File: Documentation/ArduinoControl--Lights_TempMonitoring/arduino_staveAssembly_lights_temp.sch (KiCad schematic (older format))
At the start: 31 parts, among them P1 Power, P2 Analog, P3 Digital, P4 Digital, P5 CONN_01X01, P6 CONN_01X01, P7 CONN_01X01, P8 CONN_01X01

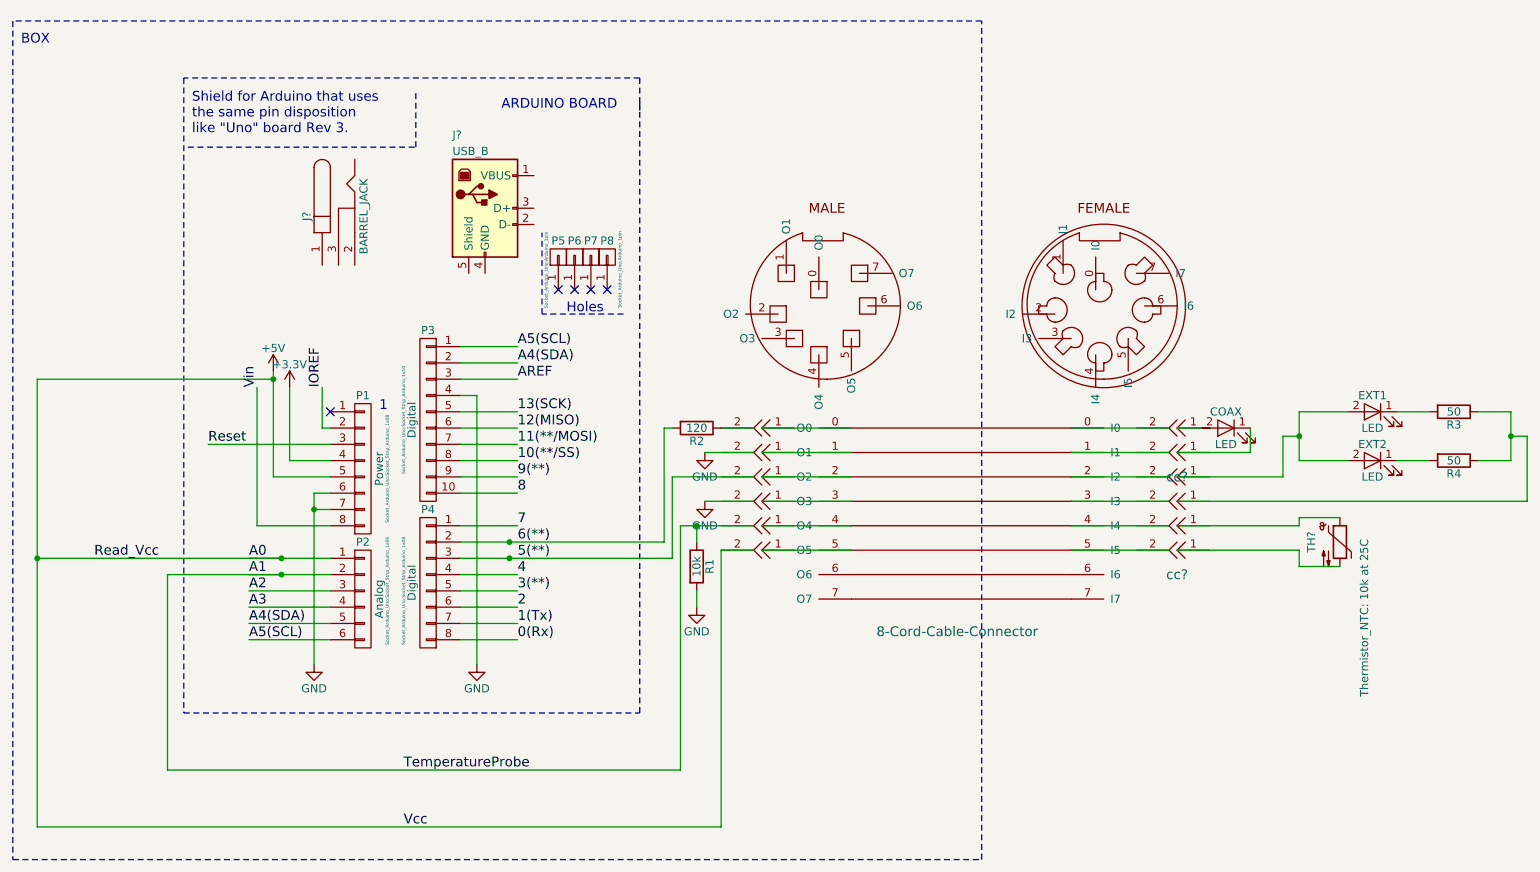
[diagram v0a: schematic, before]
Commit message: Arduino Lights system documentation
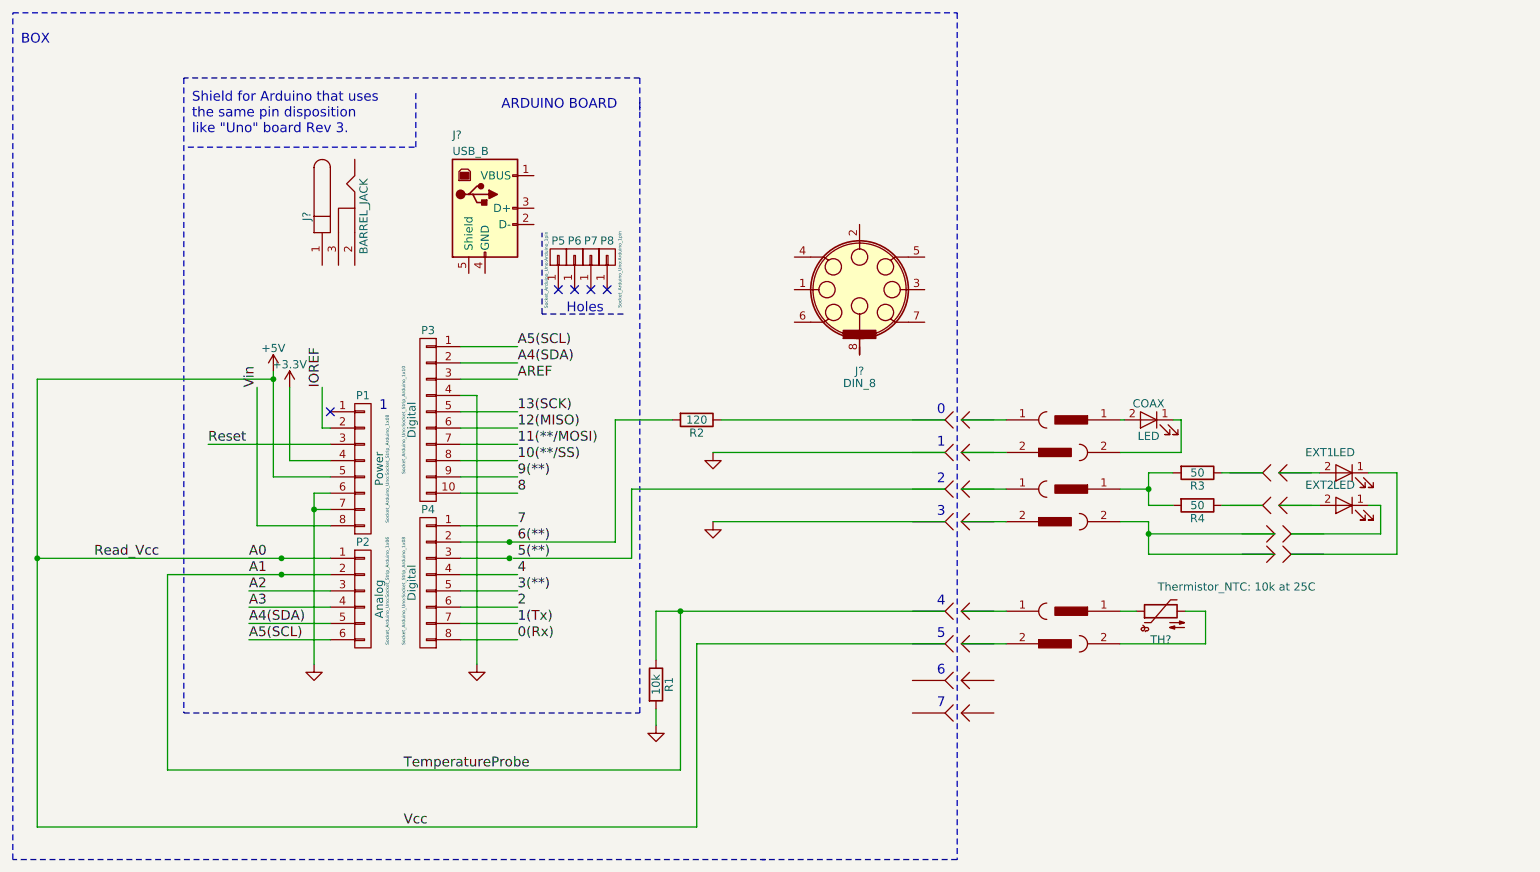
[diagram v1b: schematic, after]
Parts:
- removed U?: 8-Cord-Cable-Connector, symbol 8-Cord-Cable-Connector
- removed cc? (x12): single-wire connection, symbol Single-wire-connection
- added J?: DIN_8, symbol DIN_8
- added J? (x3): CONN_01X02_POL1, symbol CONN_01X02_POL1
- added J? (x3): CONN_01X02_POL2, symbol CONN_01X02_POL2
- added cc? (x12): Single-wire-connection-female, symbol Single-wire-connection-female
- added cc? (x12): Single-wire-connection-male, symbol Single-wire-connection-male
- COAX, EXT1, EXT2: Hotenda Part Number (none) -> H2886877
- TH?: DigiKey Part Number (none) -> 490-12820-ND
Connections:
- net +5V: now also cc?.~
- net 5(**): now also cc?.~; no longer P4.3 (P3)
- net A1: now also cc?.~
- net GND: now also cc?.~, cc?.~
- net at TH?.1: now also J?.1
- net at TH?.2: now also J?.2
- net at COAX.1 (K): now also J?.2
- net at COAX.2 (A): now also J?.1
- net at R3.1: now also cc?.~; no longer R4.1
- net at R3.2: now also R4.2, J?.1; no longer EXT1.1 (K)
- net at EXT2.1 (K): now also cc?.~; no longer R4.2
- net at EXT1.2 (A): now also cc?.~; no longer EXT2.2 (A)
- net at R2.1: now also cc?.~
- new net: R4.1, cc?.~
- new net: EXT1.1 (K), cc?.~
- new net: EXT2.2 (A), cc?.~
- new net: J?.2, cc?.~ (x3)
- new net: J?.1, cc?.~ (x3)
- new net: J?.2, cc?.~, cc?.~
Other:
- note added: "0"
- note added: "2"
- note added: "3"
- note added: "4"
- note added: "5"
- note added: "6"
- note added: "7"
- moved on the sheet: COAX, EXT1, EXT2, R1, R2, R3, R4, TH?
